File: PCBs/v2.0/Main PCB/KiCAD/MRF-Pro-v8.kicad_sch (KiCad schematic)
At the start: 4 parts, among them J1 Feather-1, J2 Feather-2, J3 FPC 8P Connector, J4 Conn_01x08

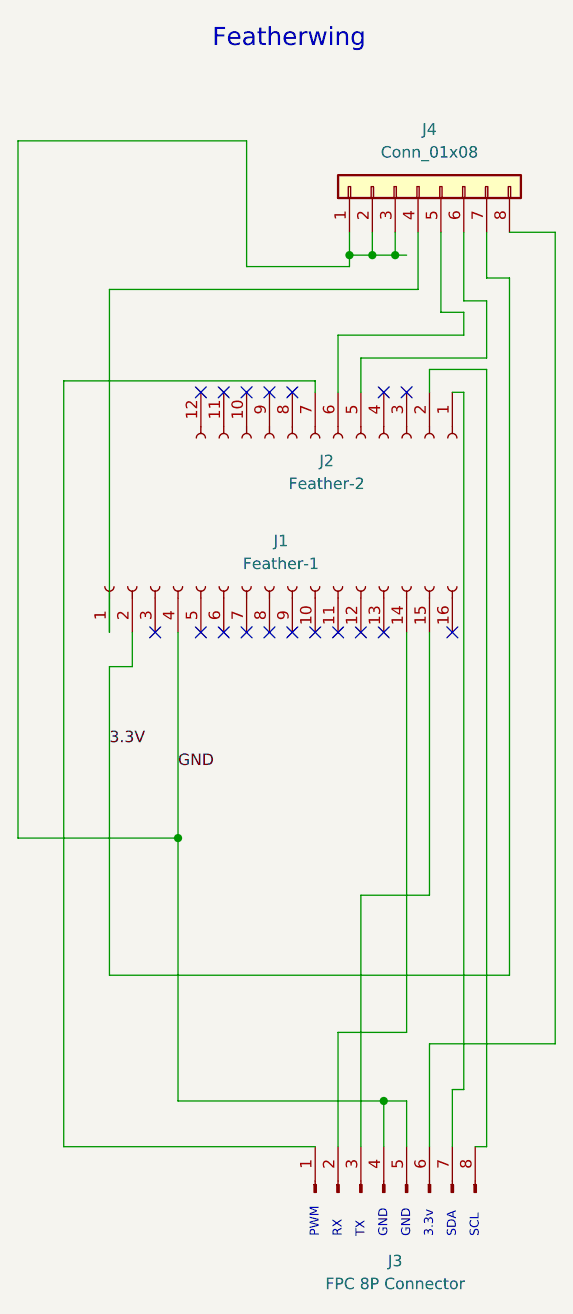
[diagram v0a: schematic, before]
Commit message: Capture dedicated LiDAR LDO in the breakout and main schematics
Breakout (MRF-Pro-v8-breakout): add U1 TLV75533 3.3V LDO with input
decoupling (Cin1 1uF, Cin2 10uF) and FB1 (0R default) splitting the
regulator output net 3V3_LIDAR from the laser bulk net 3V3_LASER.
J7 pin1 moves to 3V3_LASER (with the 47uF C1), pin2 to 3V3_LIDAR (with
C2/C3 at U1 OUT); J5 pin6 becomes VBAT feeding U1 IN; U1 EN sits on the
FPC pin1 net and U1 pin4 (NC) is flagged no-connect. C1/C2/C3 reused as
the output network. ERC clean, 0 warnings.

Main (MRF-Pro-v8): wire the Feather BAT pin (J2 pin12) to a new VBAT net
through to FPC pin6, detaching pin6 from its old J4-pin8 net and
no-connecting the freed J4 pin8. 3.3V rail unchanged. ERC: 0 errors
(one pre-existing dangling-wire warning unchanged).

Schematic capture and ERC/netlist verification only; PCB layout to follow.
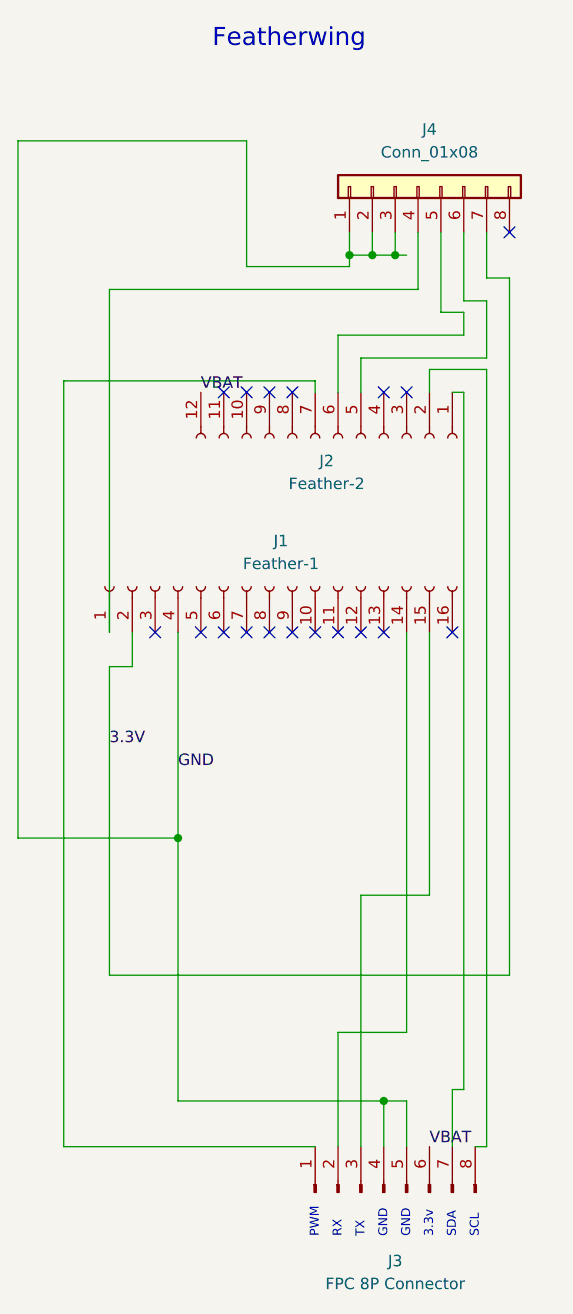
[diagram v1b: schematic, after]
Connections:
- net VBAT: now reaches J2.12 (Pin_12)
- net VBAT: now also J3.6 (Pin_6)
- net at J4.8 (Pin_8): no longer J3.6 (Pin_6)
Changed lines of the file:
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@@
 (kicad_sch
-	(version 20250114)
+	(version 20260306)
 	(generator "eeschema")
-	(generator_version "9.0")
+	(generator_version "10.0")
 	(paper "A4")
 	(text "RX"
@@
 	)
 	(no_connect
-		(at 80.01 72.39)
-	)
-	(no_connect
 		(at 85.09 99.06)
 	)
 	(no_connect
+		(at 114.3 54.61)
+	)
+	(no_connect
 		(at 102.87 72.39)
 	)
@@
 	(wire
 		(pts
-			(xy 119.38 144.78) (xy 119.38 54.61)
-		)
-		(stroke
-			(width 0)
-			(type default)
-		)
-	)
-	(wire
-		(pts
-			(xy 105.41 156.21) (xy 105.41 144.78)
-		)
-		(stroke
-			(width 0)
-			(type default)
-		)
-	)
-	(wire
-		(pts
 			(xy 85.09 58.42) (xy 96.52 58.42)
 		)
@@
 	(wire
 		(pts
-			(xy 105.41 144.78) (xy 119.38 144.78)
-		)
-		(stroke
-			(width 0)
-			(type default)
-		)
-	)
-	(wire
-		(pts
 			(xy 85.09 44.45) (xy 85.09 58.42)
 		)
@@
 		(pts
 			(xy 107.95 149.86) (xy 107.95 156.21)
-		)
-		(stroke
-			(width 0)
-			(type default)
-		)
-	)
-	(wire
-		(pts
-			(xy 119.38 54.61) (xy 114.3 54.61)
 		)
 		(stroke
@@
 			(justify left bottom)
 		)
-		(property "Netclass" "GND"
+		(property "Net Class" "GND"
 			(at 77.47 115.57 0)
+			(show_name no)
+			(do_not_autoplace no)
 			(effects
 				(font
@@
 				(justify left)
 			)
+		)
+	)
+	(label "VBAT"
+		(at 105.41 156.21 0)
+		(effects
+			(font
+				(size 1.27 1.27)
+			)
+			(justify left bottom)
+		)
+	)
+	(label "VBAT"
+		(at 80.01 72.39 0)
+		(effects
+			(font
+				(size 1.27 1.27)
+			)
+			(justify left bottom)
 		)
 	)
@@
 			(justify left bottom)
 		)
-		(property "Netclass" "3.3V"
+		(property "Net Class" "3.3V"
 			(at 69.85 113.03 0)
+			(hide yes)
+			(show_name no)
+			(do_not_autoplace no)
 			(effects
 				(font
@@
 				)
 				(justify left)
-				(hide yes)
 			)
 		)
@@
 		(at 95.25 77.47 270)
 		(unit 1)
+		(body_style 1)
 		(exclude_from_sim no)
 		(in_bom yes)
 		(on_board yes)
+		(in_pos_files yes)
 		(dnp no)
 		(fields_autoplaced yes)
 		(property "Reference" "J2"
 			(at 93.98 80.01 90)
+			(show_name no)
+			(do_not_autoplace no)
 			(effects
 				(font
@@
 		(property "Value" "Feather-2"
 			(at 93.98 82.55 90)
+			(show_name no)
+			(do_not_autoplace no)
 			(effects
 				(font
@@
 		(property "Footprint" "Connector_PinHeader_2.54mm:PinHeader_1x12_P2.54mm_Vertical"
 			(at 95.25 77.47 0)
-			(effects
-				(font
-					(size 1.27 1.27)
-				)
-				(hide yes)
-			)
-		)
-		(property "Datasheet" "~"
+			(hide yes)
+			(show_name no)
+			(do_not_autoplace no)
+			(effects
+				(font
+					(size 1.27 1.27)
+				)
+			)
+		)
+		(property "Datasheet" ""
 			(at 95.25 77.47 0)
-			(effects
-				(font
-					(size 1.27 1.27)
-				)
-				(hide yes)
+			(hide yes)
+			(show_name no)
+			(do_not_autoplace no)
+			(effects
+				(font
+					(size 1.27 1.27)
+				)
 			)
 		)
 		(property "Description" ""
 			(at 95.25 77.47 0)
+			(show_name no)
+			(do_not_autoplace no)
 			(effects
 				(font
@@
 		)
 		(instances
-			(project "MRF-Pro-v7"
+			(project "MRF-Pro-v8"
 				(path "/896eaae8-6acf-41d9-a1f7-3a80349c3bd9"
 					(reference "J2")
@@
 		(at 100.33 161.29 90)
 		(unit 1)
+		(body_style 1)
 		(exclude_from_sim no)
 		(in_bom yes)
 		(on_board yes)
+		(in_pos_files yes)
 		(dnp no)
 		(property "Reference" "J3"
 			(at 101.6 168.91 90)
+			(show_name no)
+			(do_not_autoplace no)
 			(effects
 				(font
@@
 		(property "Value" "FPC 8P Connector"
 			(at 101.6 171.45 90)
+			(show_name no)
+			(do_not_autoplace no)
 			(effects
 				(font
@@
 		(property "Footprint" "Connector_FFC-FPC:TE_0-1734839-8_1x08-1MP_P0.5mm_Horizontal"
 			(at 100.33 161.29 0)
-			(effects
-				(font
-					(size 1.27 1.27)
-				)
-				(hide yes)
-			)
-		)
-		(property "Datasheet" "~"
+			(hide yes)
+			(show_name no)
+			(do_not_autoplace no)
+			(effects
+				(font
+					(size 1.27 1.27)
+				)
+			)
+		)
+		(property "Datasheet" ""
 			(at 100.33 161.29 0)
-			(effects
-				(font
-					(size 1.27 1.27)
-				)
-				(hide yes)
+			(hide yes)
+			(show_name no)
+			(do_not_autoplace no)
+			(effects
+				(font
+					(size 1.27 1.27)
+				)
 			)
 		)
 		(property "Description" ""
 			(at 100.33 161.29 0)
+			(show_name no)
+			(do_not_autoplace no)
 			(effects
 				(font
@@
 		(property "LCSC" "C2856797"
 			(at 100.33 161.29 90)
-			(effects
-				(font
-					(size 1.27 1.27)
-				)
-				(hide yes)
+			(hide yes)
+			(show_name no)
+			(do_not_autoplace no)
+			(effects
+				(font
+					(size 1.27 1.27)
+				)
 			)
 		)
@@
 		)
 		(instances
-			(project "MRF-Pro-v7"
+			(project "MRF-Pro-v8"
 				(path "/896eaae8-6acf-41d9-a1f7-3a80349c3bd9"
 					(reference "J3")
@@
 		(at 104.14 49.53 90)
 		(unit 1)
+		(body_style 1)
 		(exclude_from_sim no)
 		(in_bom yes)
 		(on_board yes)
+		(in_pos_files yes)
 		(dnp no)
 		(fields_autoplaced yes)
 		(property "Reference" "J4"
 			(at 105.41 43.18 90)
+			(show_name no)
+			(do_not_autoplace no)
 			(effects
 				(font
@@
 		(property "Value" "Conn_01x08"
 			(at 105.41 45.72 90)
+			(show_name no)
+			(do_not_autoplace no)
 			(effects
 				(font
@@
 		(property "Footprint" "Connector_JST:JST_SH_BM08B-SRSS-TB_1x08-1MP_P1.00mm_Vertical"
 			(at 104.14 49.53 0)
-			(effects
-				(font
-					(size 1.27 1.27)
-				)
-				(hide yes)
-			)
-		)
-		(property "Datasheet" "~"
+			(hide yes)
+			(show_name no)
+			(do_not_autoplace no)
+			(effects
+				(font
+					(size 1.27 1.27)
+				)
+			)
+		)
+		(property "Datasheet" ""
 			(at 104.14 49.53 0)
-			(effects
-				(font
-					(size 1.27 1.27)
-				)
-				(hide yes)
+			(hide yes)
+			(show_name no)
+			(do_not_autoplace no)
+			(effects
+				(font
+					(size 1.27 1.27)
+				)
 			)
 		)
 		(property "Description" "Generic connector, single row, 01x08, script generated (kicad-library-utils/schlib/autogen/connector/)"
 			(at 104.14 49.53 0)
-			(effects
-				(font
-					(size 1.27 1.27)
-				)
-				(hide yes)
+			(hide yes)
+			(show_name no)
+			(do_not_autoplace no)
+			(effects
+				(font
+					(size 1.27 1.27)
+				)
 			)
 		)
 		(property "LCSC" "C7430448"
 			(at 104.14 49.53 90)
-			(effects
-				(font
-					(size 1.27 1.27)
-				)
-				(hide yes)
+			(hide yes)
+			(show_name no)
+			(do_not_autoplace no)
+			(effects
+				(font
+					(size 1.27 1.27)
+				)
 			)
 		)
@@
 		)
 		(instances
-			(project "MRF-Pro-v7"
+			(project "MRF-Pro-v8"
 				(path "/896eaae8-6acf-41d9-a1f7-3a80349c3bd9"
 					(reference "J4")
@@
 		(at 87.63 93.98 90)
 		(unit 1)
+		(body_style 1)
 		(exclude_from_sim no)
 		(in_bom yes)
 		(on_board yes)
+		(in_pos_files yes)
 		(dnp no)
 		(fields_autoplaced yes)
 		(property "Reference" "J1"
 			(at 88.9 88.9 90)
+			(show_name no)
+			(do_not_autoplace no)
 			(effects
 				(font
@@
 		(property "Value" "Feather-1"
 			(at 88.9 91.44 90)
+			(show_name no)
+			(do_not_autoplace no)
 			(effects
 				(font
@@
 		(property "Footprint" "Connector_PinHeader_2.54mm:PinHeader_1x16_P2.54mm_Vertical"
 			(at 87.63 93.98 0)
-			(effects
-				(font
-					(size 1.27 1.27)
-				)
-				(hide yes)
-			)
-		)
-		(property "Datasheet" "~"
+			(hide yes)
+			(show_name no)
+			(do_not_autoplace no)
+			(effects
+				(font
+					(size 1.27 1.27)
+				)
+			)
+		)
+		(property "Datasheet" ""
 			(at 87.63 93.98 0)
-			(effects
-				(font
-					(size 1.27 1.27)
-				)
-				(hide yes)
+			(hide yes)
+			(show_name no)
+			(do_not_autoplace no)
+			(effects
+				(font
+					(size 1.27 1.27)
+				)
 			)
 		)
 		(property "Description" ""
 			(at 87.63 93.98 0)
+			(show_name no)
+			(do_not_autoplace no)
 			(effects
 				(font
@@
 		)
 		(instances
-			(project "MRF-Pro-v7"
+			(project "MRF-Pro-v8"
 				(path "/896eaae8-6acf-41d9-a1f7-3a80349c3bd9"
 					(reference "J1")

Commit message: Rework the main-board power switch as a J4 DPDT and lay out the board
The power switch moves onto the 8-pin J4 header as a DPDT: pole A
gates the Feather 3.3V onto the switched rail 3V3_SW (FPC pin 1),
pole B pulls Feather EN to GND when off, holding the MCU off. This
fixes the prior topology where FPC pin 1 ran from a GPIO (D11) and the
Feather 3.3V never reached the FPC. Feather BAT now drives VBAT to FPC
pin 6 for the breakout LDO. Routed to match; D11 and RST are freed.
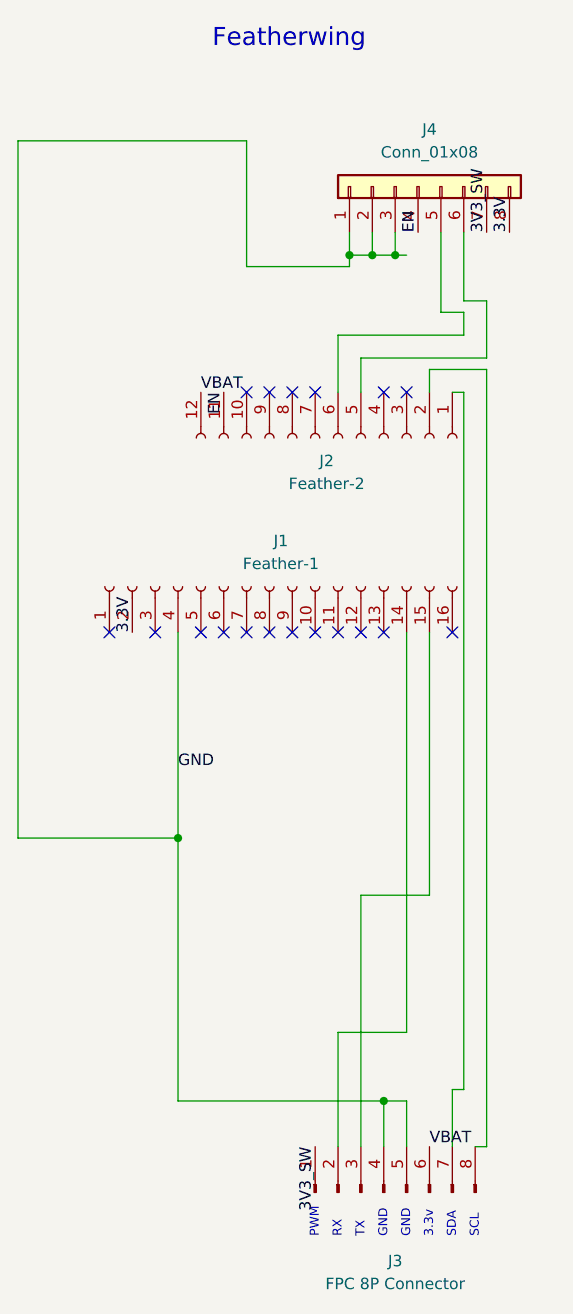
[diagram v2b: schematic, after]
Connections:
- net 3.3V: now also J4.8 (Pin_8); no longer J4.7 (Pin_7)
- net EN: now reaches J2.11 (Pin_11)
- net EN: now also J4.4 (Pin_4)
- net at J2.7 (Pin_7): no longer J3.1 (Pin_1)
- net at J1.1 (Pin_1): no longer J4.4 (Pin_4)
- new net 3V3_SW: J3.1 (Pin_1), J4.7 (Pin_7)
